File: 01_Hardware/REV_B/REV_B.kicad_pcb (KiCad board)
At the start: 2 copper layers, 65 x 30 mm, 79 parts, among them J1 RaspberryPi, J10 Conn_01x03, J11 Conn_01x03, J12 Conn_01x03, J13 Conn_01x08, J2 Conn_01x02, J3 Conn_01x02, J4 Conn_01x02, J5 Conn_01x08, J6 Conn_02x04_Counter_Clockwise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

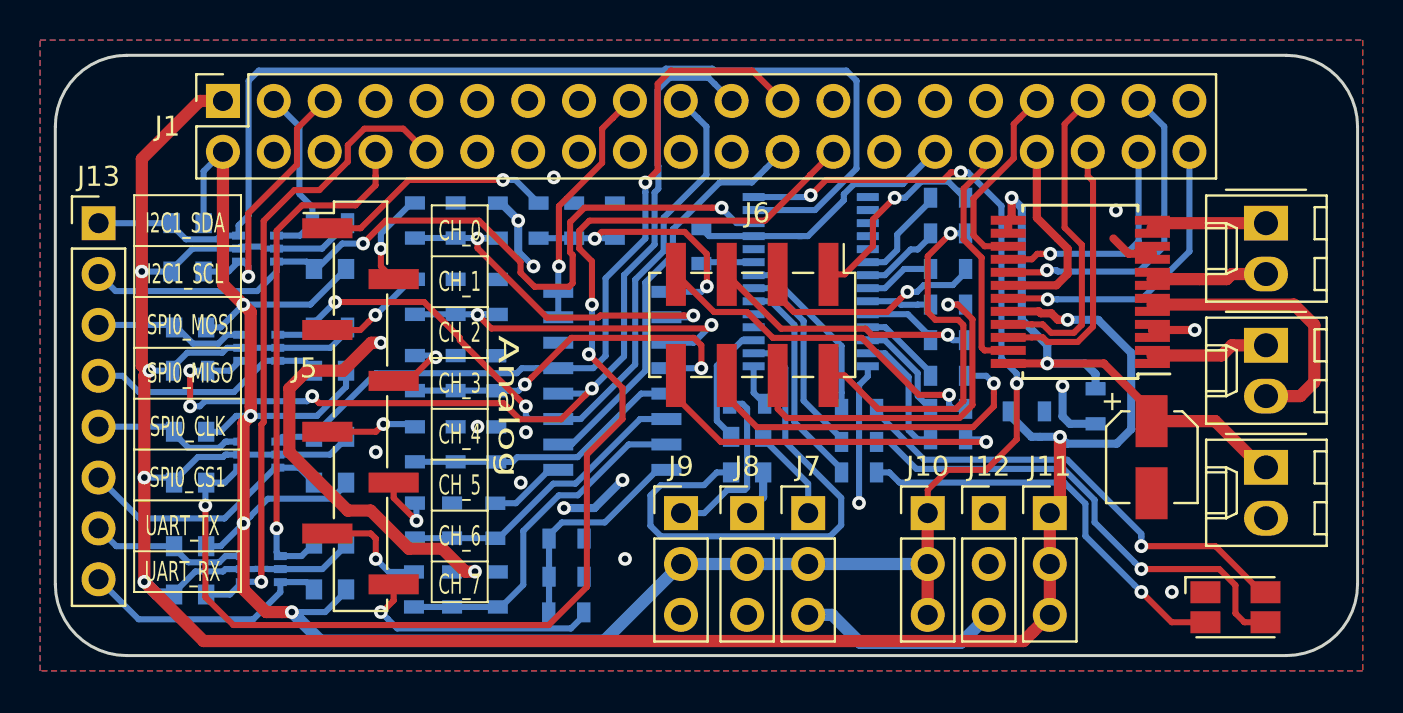
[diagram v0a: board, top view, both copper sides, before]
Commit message: Taster added. routing not done
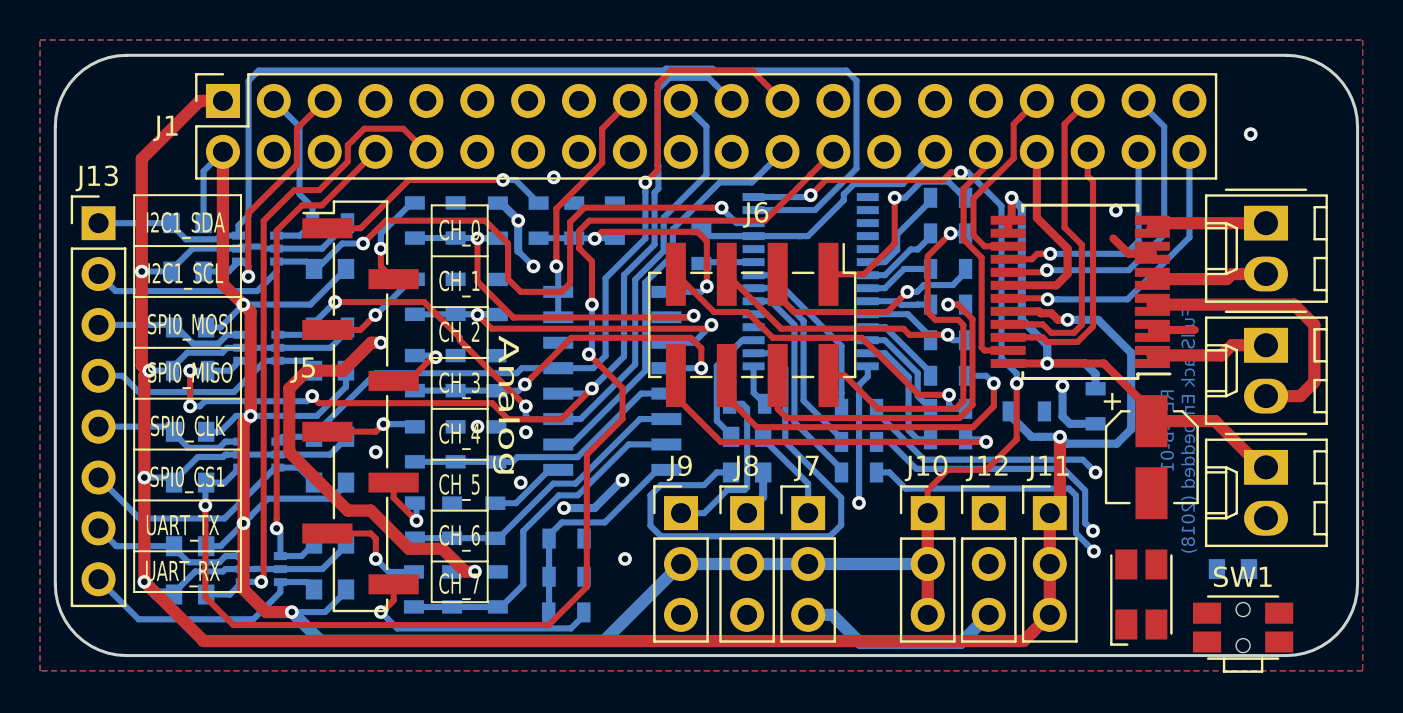
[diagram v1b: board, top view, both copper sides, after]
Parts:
- added R48: 1k, Resistor_SMD:R_0603_1608Metric, B.Cu at (58.8, 25.7)
- added SW1: SW_Push, Button_Switch_SMD:SW_SPST_EVQP7C, F.Cu at (59.3, 28.6)
- moved D1 4.74 mm to (54.2, 26.9), turned to 90 degrees
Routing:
- net Net-(D1-Pad2): track 23.7 -> 12.3 mm
- net Net-(D1-Pad3): track 24.6 -> 13.6 mm
- net Net-(D1-Pad4): track 20.6 -> 13.6 mm
- net Net-(C5-Pad1): track 19.3 -> 20.3 mm
- net UART_TX_LV: track 25.8 -> 24.8 mm
- net I2C1_SCL_HV: track 40.7 -> 41.5 mm
- net Net-(J6-Pad1): track 9.87 -> 10.4 mm
- net Net-(J1-Pad37): track 16.5 -> 15.9 mm
- net GND: vias 17 -> 16
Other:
- board text added: "REV-B-01 FullStack Embedded (2018)"
